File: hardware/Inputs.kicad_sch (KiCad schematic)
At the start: 34 parts, among them J13 Conn_01x05, J14 Conn_01x05, J15 Conn_01x05, J16 Conn_01x05, J17 Conn_01x05, J18 Conn_01x05, J19 Conn_01x03, J20 Conn_01x03, J21 Conn_01x03, J22 Conn_01x03, J23 Conn_01x03, J24 Conn_01x03, J25 Conn_01x02, J26 Conn_01x02, J27 FTSH-107-01-L-D-K

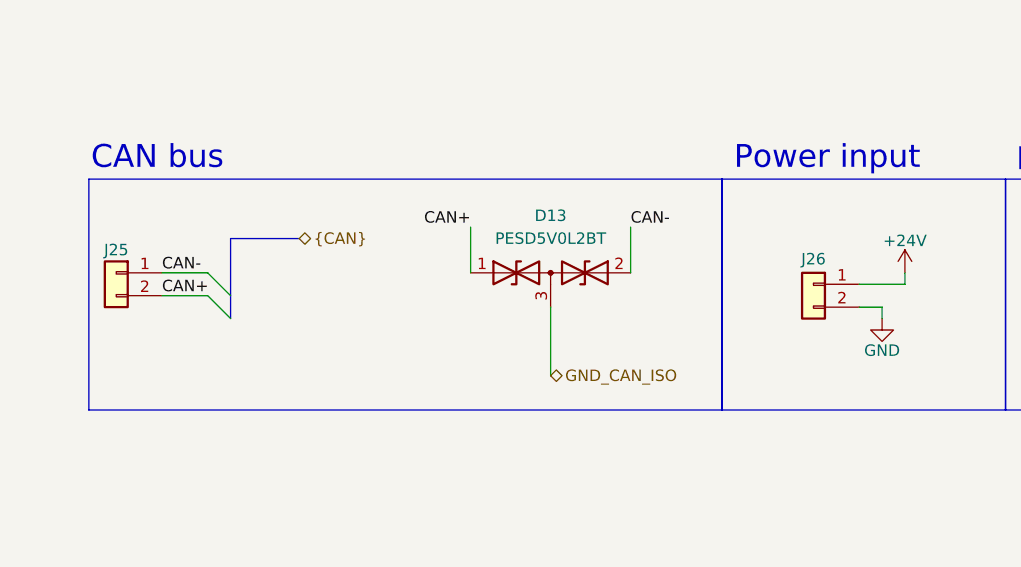
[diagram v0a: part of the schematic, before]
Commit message: Finished components placement on PCB
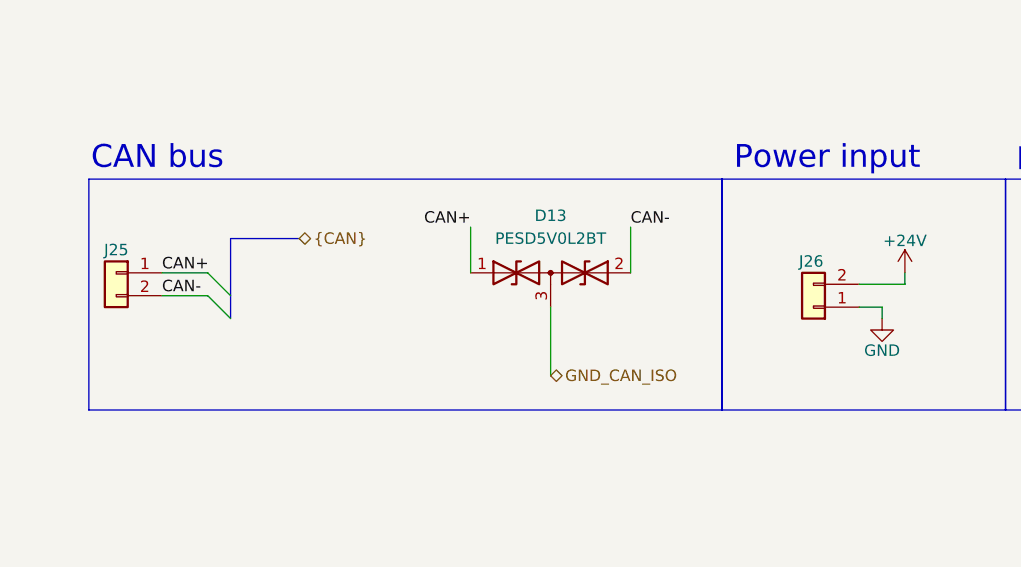
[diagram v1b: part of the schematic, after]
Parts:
- J25, J26: footprint Wago_01x02:26011102 -> StrainRelief:Wire_StrainRelief
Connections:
- net +24V: now also J26.2 (Pin_2); no longer J26.1 (Pin_1)
- net CAN+: now also J25.1 (Pin_1); no longer J25.2 (Pin_2)
- net CAN-: now also J25.2 (Pin_2); no longer J25.1 (Pin_1)
- net GND: now also J26.1 (Pin_1); no longer J26.2 (Pin_2)
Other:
- moved on the sheet: J26
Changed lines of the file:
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@@
 	(wire
 		(pts
+			(xy 190.5 160.02) (xy 195.58 160.02)
+		)
+		(stroke
+			(width 0)
+			(type default)
+		)
+	)
+	(wire
+		(pts
 			(xy 302.26 82.55) (xy 302.26 85.09)
 		)
@@
 	(wire
 		(pts
-			(xy 190.5 160.02) (xy 195.58 160.02)
-		)
-		(stroke
-			(width 0)
-			(type default)
-		)
-	)
-	(wire
-		(pts
-			(xy 190.5 162.56) (xy 195.58 162.56)
+			(xy 267.97 161.29) (xy 273.05 161.29)
 		)
 		(stroke
@@
 		)
 	)
-	(wire
-		(pts
-			(xy 267.97 163.83) (xy 270.51 163.83)
-		)
-		(stroke
-			(width 0)
-			(type default)
-		)
-	)
 	(bus
 		(pts
@@
 	(wire
 		(pts
+			(xy 267.97 163.83) (xy 270.51 163.83)
+		)
+		(stroke
+			(width 0)
+			(type default)
+		)
+	)
+	(wire
+		(pts
 			(xy 80.01 212.09) (xy 87.63 212.09)
 		)
@@
 		)
 	)
-	(wire
-		(pts
-			(xy 267.97 161.29) (xy 273.05 161.29)
-		)
-		(stroke
-			(width 0)
-			(type default)
-		)
-	)
 	(bus
 		(pts
@@
 	(wire
 		(pts
+			(xy 190.5 162.56) (xy 195.58 162.56)
+		)
+		(stroke
+			(width 0)
+			(type default)
+		)
+	)
+	(wire
+		(pts
 			(xy 101.6 109.22) (xy 105.41 109.22)
 		)
@@
 	)
 	(label "CAN-"
-		(at 190.5 160.02 0)
+		(at 190.5 162.56 0)
 		(effects
 			(font
@@
 	)
 	(label "CAN+"
-		(at 190.5 162.56 0)
+		(at 190.5 160.02 0)
 		(effects
 			(font
@@
 			)
 		)
-		(property "Datasheet" "https://wago.priintcloud.com/datasheets/2604-1103/en/b87bf34972496b0cc9989b5aee7282f1?attempt=1&signature=9e2143c2bdc0f032c541ec220a7d0518_1h3r4vhsf"
+		(property "Datasheet" "https://wago.priintcloud.com/datasheets/2601-1103/en/d41d8cd98f00b204e9800998ecf8427e?attempt=1&signature=00012c5e7a2599b3d4b70dcfe3f90a33_1jis4hf1d"
 			(at 24.13 186.69 0)
 			(effects
@@
 			)
 		)
-		(property "Datasheet" "https://wago.priintcloud.com/datasheets/2604-1105/en/b87bf34972496b0cc9989b5aee7282f1?attempt=1&signature=9e2143c2bdc0f032c541ec220a7d0518_1h3r4vhsf"
+		(property "Datasheet" "https://wago.priintcloud.com/datasheets/2601-1105/en/d41d8cd98f00b204e9800998ecf8427e?attempt=1&signature=731afa92f4ad419acfaed54798e1c80c_1jis4e336"
 			(at 96.52 104.14 0)
 			(effects
@@
 			)
 		)
-		(property "Datasheet" "https://wago.priintcloud.com/datasheets/2604-1103/en/b87bf34972496b0cc9989b5aee7282f1?attempt=1&signature=9e2143c2bdc0f032c541ec220a7d0518_1h3r4vhsf"
+		(property "Datasheet" "https://wago.priintcloud.com/datasheets/2601-1103/en/d41d8cd98f00b204e9800998ecf8427e?attempt=1&signature=00012c5e7a2599b3d4b70dcfe3f90a33_1jis4hf1d"
 			(at 24.13 161.29 0)
 			(effects
@@
 		(lib_name "Conn_01x02_1")
 		(lib_id "Connector_Generic:Conn_01x02")
-		(at 262.89 161.29 0)
-		(mirror y)
+		(at 262.89 163.83 180)
 		(unit 1)
 		(exclude_from_sim no)
@@
 		(dnp no)
 		(property "Reference" "J26"
-			(at 262.89 158.496 0)
+			(at 262.636 158.75 0)
 			(effects
 				(font
@@
 		)
 		(property "Value" "Conn_01x02"
-			(at 262.89 167.64 0)
+			(at 262.89 157.48 0)
 			(effects
 				(font
@@
 			)
 		)
-		(property "Footprint" "Wago_01x02:26011102"
-			(at 262.89 161.29 0)
+		(property "Footprint" "StrainRelief:Wire_StrainRelief"
+			(at 262.89 163.83 0)
 			(effects
 				(font
@@
 			)
 		)
-		(property "Datasheet" "https://wago.priintcloud.com/datasheets/2604-1102/en/b87bf34972496b0cc9989b5aee7282f1?attempt=1&signature=9e2143c2bdc0f032c541ec220a7d0518_1h3r4vhsf"
-			(at 262.89 161.29 0)
+		(property "Datasheet" "-"
+			(at 262.89 163.83 0)
 			(effects
 				(font
@@
 		)
 		(property "Description" "Power input"
-			(at 262.89 161.29 0)
+			(at 262.89 163.83 0)
 			(effects
 				(font
@@
 			)
 		)
-		(property "Datasheet" "https://wago.priintcloud.com/datasheets/2604-1103/en/b87bf34972496b0cc9989b5aee7282f1?attempt=1&signature=9e2143c2bdc0f032c541ec220a7d0518_1h3r4vhsf"
+		(property "Datasheet" "https://wago.priintcloud.com/datasheets/2601-1103/en/d41d8cd98f00b204e9800998ecf8427e?attempt=1&signature=00012c5e7a2599b3d4b70dcfe3f90a33_1jis4hf1d"
 			(at 74.93 212.09 0)
 			(effects
@@
 			)
 		)
-		(property "Datasheet" "https://wago.priintcloud.com/datasheets/2604-1105/en/b87bf34972496b0cc9989b5aee7282f1?attempt=1&signature=9e2143c2bdc0f032c541ec220a7d0518_1h3r4vhsf"
+		(property "Datasheet" "https://wago.priintcloud.com/datasheets/2601-1105/en/d41d8cd98f00b204e9800998ecf8427e?attempt=1&signature=731afa92f4ad419acfaed54798e1c80c_1jis4e336"
 			(at 35.56 104.14 0)
 			(effects
@@
 			)
 		)
-		(property "Datasheet" "https://wago.priintcloud.com/datasheets/2604-1105/en/b87bf34972496b0cc9989b5aee7282f1?attempt=1&signature=9e2143c2bdc0f032c541ec220a7d0518_1h3r4vhsf"
+		(property "Datasheet" "https://wago.priintcloud.com/datasheets/2601-1105/en/d41d8cd98f00b204e9800998ecf8427e?attempt=1&signature=731afa92f4ad419acfaed54798e1c80c_1jis4e336"
 			(at 35.56 35.56 0)
 			(effects
@@
 			)
 		)
-		(property "Footprint" "Wago_01x02:26011102"
+		(property "Footprint" "StrainRelief:Wire_StrainRelief"
 			(at 185.42 160.02 0)
 			(effects
@@
 			)
 		)
-		(property "Datasheet" "https://wago.priintcloud.com/datasheets/2604-1102/en/b87bf34972496b0cc9989b5aee7282f1?attempt=1&signature=9e2143c2bdc0f032c541ec220a7d0518_1h3r4vhsf"
+		(property "Datasheet" "-"
 			(at 185.42 160.02 0)
 			(effects
@@
 			)
 		)
-		(property "Datasheet" "https://wago.priintcloud.com/datasheets/2604-1105/en/b87bf34972496b0cc9989b5aee7282f1?attempt=1&signature=9e2143c2bdc0f032c541ec220a7d0518_1h3r4vhsf"
+		(property "Datasheet" "https://wago.priintcloud.com/datasheets/2601-1105/en/d41d8cd98f00b204e9800998ecf8427e?attempt=1&signature=731afa92f4ad419acfaed54798e1c80c_1jis4e336"
 			(at 35.56 68.58 0)
 			(effects
@@
 			)
 		)
-		(property "Datasheet" "https://wago.priintcloud.com/datasheets/2604-1103/en/b87bf34972496b0cc9989b5aee7282f1?attempt=1&signature=9e2143c2bdc0f032c541ec220a7d0518_1h3r4vhsf"
+		(property "Datasheet" "https://wago.priintcloud.com/datasheets/2601-1103/en/d41d8cd98f00b204e9800998ecf8427e?attempt=1&signature=00012c5e7a2599b3d4b70dcfe3f90a33_1jis4hf1d"
 			(at 74.93 186.69 0)
 			(effects
@@
 			)
 		)
-		(property "Datasheet" "https://wago.priintcloud.com/datasheets/2604-1103/en/b87bf34972496b0cc9989b5aee7282f1?attempt=1&signature=9e2143c2bdc0f032c541ec220a7d0518_1h3r4vhsf"
+		(property "Datasheet" "https://wago.priintcloud.com/datasheets/2601-1103/en/d41d8cd98f00b204e9800998ecf8427e?attempt=1&signature=00012c5e7a2599b3d4b70dcfe3f90a33_1jis4hf1d"
 			(at 24.13 212.09 0)
 			(effects
@@
 			)
 		)
-		(property "Datasheet" "https://wago.priintcloud.com/datasheets/2604-1105/en/b87bf34972496b0cc9989b5aee7282f1?attempt=1&signature=9e2143c2bdc0f032c541ec220a7d0518_1h3r4vhsf"
+		(property "Datasheet" "https://wago.priintcloud.com/datasheets/2601-1105/en/d41d8cd98f00b204e9800998ecf8427e?attempt=1&signature=731afa92f4ad419acfaed54798e1c80c_1jis4e336"
 			(at 96.52 35.56 0)
 			(effects
@@
 			)
 		)
-		(property "Datasheet" "https://wago.priintcloud.com/datasheets/2604-1103/en/b87bf34972496b0cc9989b5aee7282f1?attempt=1&signature=9e2143c2bdc0f032c541ec220a7d0518_1h3r4vhsf"
+		(property "Datasheet" "https://wago.priintcloud.com/datasheets/2601-1103/en/d41d8cd98f00b204e9800998ecf8427e?attempt=1&signature=00012c5e7a2599b3d4b70dcfe3f90a33_1jis4hf1d"
 			(at 74.93 161.29 0)
 			(effects
@@
 			)
 		)
-		(property "Datasheet" "https://wago.priintcloud.com/datasheets/2604-1105/en/b87bf34972496b0cc9989b5aee7282f1?attempt=1&signature=9e2143c2bdc0f032c541ec220a7d0518_1h3r4vhsf"
+		(property "Datasheet" "https://wago.priintcloud.com/datasheets/2601-1105/en/d41d8cd98f00b204e9800998ecf8427e?attempt=1&signature=731afa92f4ad419acfaed54798e1c80c_1jis4e336"
 			(at 96.52 68.58 0)
 			(effects

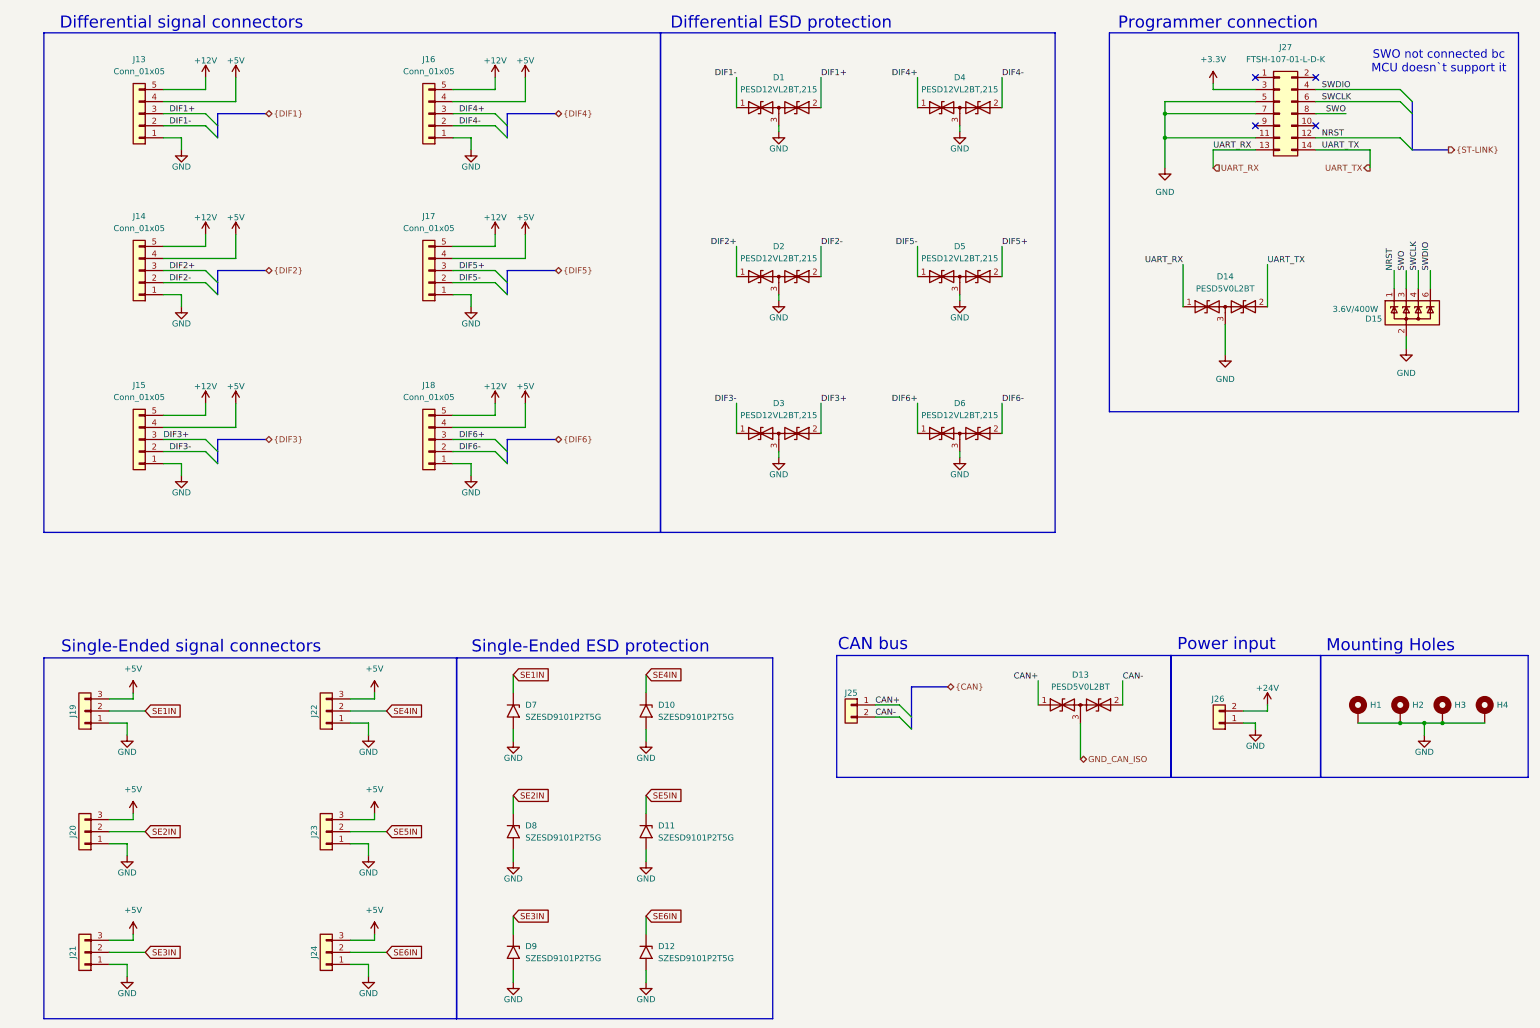
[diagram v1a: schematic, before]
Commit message: Finished routing on PCB
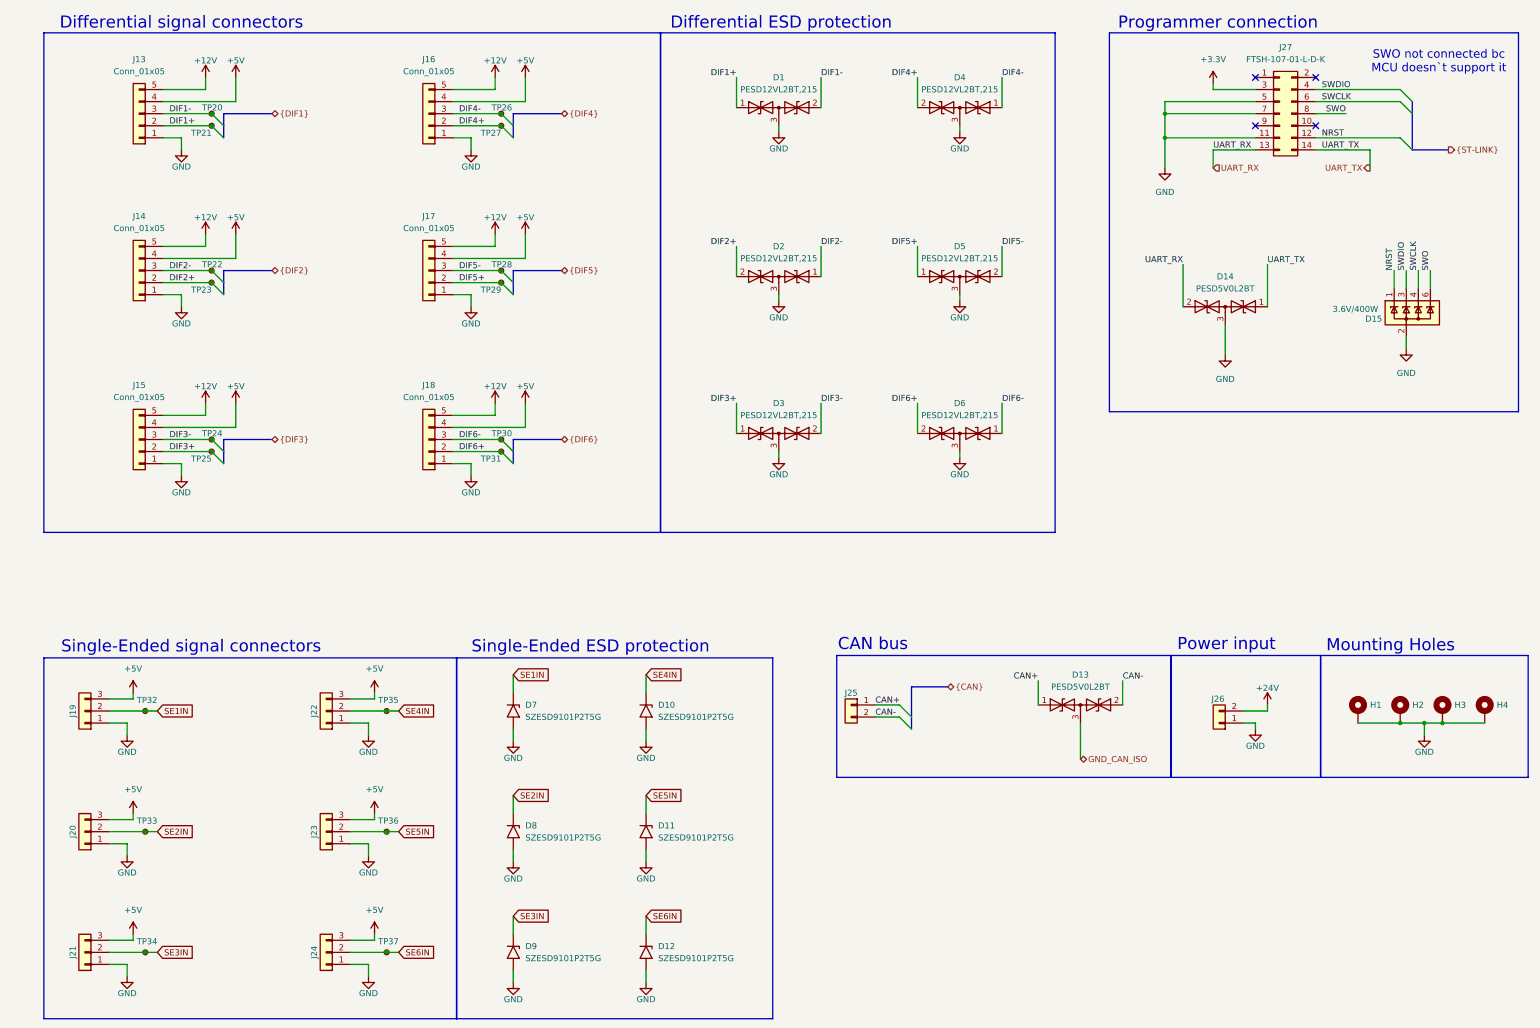
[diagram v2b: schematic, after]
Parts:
- added TP20, TP21, TP22, TP23, TP24, TP25, TP26, TP27, TP28, TP29, TP30, TP31, TP32, TP33, TP34, TP35, TP36, TP37: TestPoint_Small, TestPoint:TestPoint_THTPad_D1.0mm_Drill0.5mm, symbol Connector:TestPoint_Small
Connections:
- net DIF1+: now also D1.1 (A1), J13.2 (Pin_2), TP21.1; no longer D1.2 (A2), J13.3 (Pin_3)
- net DIF1-: now also D1.2 (A2), J13.3 (Pin_3), TP20.1; no longer D1.1 (A1), J13.2 (Pin_2)
- net DIF2+: now also D2.2 (A2), J14.2 (Pin_2), TP23.1; no longer D2.1 (A1), J14.3 (Pin_3)
- net DIF2-: now also D2.1 (A1), J14.3 (Pin_3), TP22.1; no longer D2.2 (A2), J14.2 (Pin_2)
- net DIF3+: now also D3.1 (A1), J15.2 (Pin_2), TP25.1; no longer D3.2 (A2), J15.3 (Pin_3)
- net DIF3-: now also D3.2 (A2), J15.3 (Pin_3), TP24.1; no longer D3.1 (A1), J15.2 (Pin_2)
- net DIF4+: now also D4.2 (A2), J16.2 (Pin_2), TP27.1; no longer D4.1 (A1), J16.3 (Pin_3)
- net DIF4-: now also D4.1 (A1), J16.3 (Pin_3), TP26.1; no longer D4.2 (A2), J16.2 (Pin_2)
- net DIF5+: now also D5.1 (A1), J17.2 (Pin_2), TP29.1; no longer D5.2 (A2), J17.3 (Pin_3)
- net DIF5-: now also D5.2 (A2), J17.3 (Pin_3), TP28.1; no longer D5.1 (A1), J17.2 (Pin_2)
- net DIF6+: now also D6.2 (A2), J18.2 (Pin_2), TP31.1; no longer D6.1 (A1), J18.3 (Pin_3)
- net DIF6-: now also D6.1 (A1), J18.3 (Pin_3), TP30.1; no longer D6.2 (A2), J18.2 (Pin_2)
- net SE1IN: now also TP32.1
- net SE2IN: now also TP33.1
- net SE3IN: now also TP34.1
- net SE4IN: now also TP35.1
- net SE5IN: now also TP36.1
- net SE6IN: now also TP37.1
- net SWDIO: now also D15.3 (K); no longer D15.6 (K)
- net SWO: now also D15.6 (K); no longer D15.3 (K)
- net UART_RX: now also D14.2 (A2); no longer D14.1 (A1)
- net UART_TX: now also D14.1 (A1); no longer D14.2 (A2)

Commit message: Added description, fixed engineering fee
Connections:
- net DIF1+: now also TP20.1; no longer TP21.1
- net DIF1-: now also TP21.1; no longer TP20.1
- net DIF3+: now also TP24.1; no longer TP25.1
- net DIF3-: now also TP25.1; no longer TP24.1
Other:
- moved on the sheet: TP20, TP21, TP24, TP25
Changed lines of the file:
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@@
 	)
 	(junction
-		(at 50.8 38.1)
-		(diameter 0)
-		(color 0 0 0 0)
-	)
-	(junction
 		(at 309.88 163.83)
 		(diameter 0)
@@
 	)
 	(junction
-		(at 50.8 106.68)
+		(at 36.83 161.29)
 		(diameter 0)
 		(color 0 0 0 0)
 	)
 	(junction
-		(at 36.83 161.29)
+		(at 50.8 35.56)
 		(diameter 0)
 		(color 0 0 0 0)
@@
 	)
 	(junction
+		(at 50.8 104.14)
+		(diameter 0)
+		(color 0 0 0 0)
+	)
+	(junction
 		(at 111.76 68.58)
 		(diameter 0)
@@
 	)
 	(junction
-		(at 111.76 35.56)
+		(at 50.8 38.1)
 		(diameter 0)
 		(color 0 0 0 0)
 	)
 	(junction
-		(at 50.8 104.14)
+		(at 111.76 35.56)
 		(diameter 0)
 		(color 0 0 0 0)
 	)
 	(junction
-		(at 111.76 106.68)
+		(at 50.8 106.68)
 		(diameter 0)
 		(color 0 0 0 0)
 	)
 	(junction
-		(at 50.8 35.56)
+		(at 111.76 106.68)
 		(diameter 0)
 		(color 0 0 0 0)
@@
 	(symbol
 		(lib_id "Connector:TestPoint_Small")
-		(at 50.8 104.14 0)
+		(at 50.8 106.68 0)
 		(unit 1)
 		(exclude_from_sim no)
@@
 		(dnp no)
 		(property "Reference" "TP24"
-			(at 48.768 102.87 0)
+			(at 45.974 108.204 0)
 			(effects
 				(font
@@
 		)
 		(property "Value" "TestPoint_Small"
-			(at 52.07 105.4099 0)
+			(at 52.07 107.9499 0)
 			(effects
 				(font
@@
 		)
 		(property "Footprint" "TestPoint:TestPoint_THTPad_D1.0mm_Drill0.5mm"
-			(at 55.88 104.14 0)
+			(at 55.88 106.68 0)
 			(effects
 				(font
@@
 		)
 		(property "Datasheet" "~"
-			(at 55.88 104.14 0)
+			(at 55.88 106.68 0)
 			(effects
 				(font
@@
 		)
 		(property "Description" "test point"
-			(at 50.8 104.14 0)
+			(at 50.8 106.68 0)
 			(effects
 				(font
@@
 	(symbol
 		(lib_id "Connector:TestPoint_Small")
-		(at 50.8 35.56 0)
+		(at 50.8 38.1 0)
 		(unit 1)
 		(exclude_from_sim no)
@@
 		(dnp no)
 		(property "Reference" "TP20"
-			(at 48.768 34.29 0)
+			(at 46.228 39.624 0)
 			(effects
 				(font
@@
 		)
 		(property "Value" "TestPoint_Small"
-			(at 52.07 36.8299 0)
+			(at 52.07 39.3699 0)
 			(effects
 				(font
@@
 		)
 		(property "Footprint" "TestPoint:TestPoint_THTPad_D1.0mm_Drill0.5mm"
-			(at 55.88 35.56 0)
+			(at 55.88 38.1 0)
 			(effects
 				(font
@@
 		)
 		(property "Datasheet" "~"
-			(at 55.88 35.56 0)
+			(at 55.88 38.1 0)
 			(effects
 				(font
@@
 		)
 		(property "Description" "test point"
-			(at 50.8 35.56 0)
+			(at 50.8 38.1 0)
 			(effects
 				(font
@@
 	(symbol
 		(lib_id "Connector:TestPoint_Small")
-		(at 50.8 106.68 0)
+		(at 50.8 104.14 0)
 		(unit 1)
 		(exclude_from_sim no)
@@
 		(dnp no)
 		(property "Reference" "TP25"
-			(at 46.482 108.204 0)
+			(at 48.514 102.616 0)
 			(effects
 				(font
@@
 		)
 		(property "Value" "TestPoint_Small"
-			(at 52.07 107.9499 0)
+			(at 52.07 105.4099 0)
 			(effects
 				(font
@@
 		)
 		(property "Footprint" "TestPoint:TestPoint_THTPad_D1.0mm_Drill0.5mm"
-			(at 55.88 106.68 0)
+			(at 55.88 104.14 0)
 			(effects
 				(font
@@
 		)
 		(property "Datasheet" "~"
-			(at 55.88 106.68 0)
+			(at 55.88 104.14 0)
 			(effects
 				(font
@@
 		)
 		(property "Description" "test point"
-			(at 50.8 106.68 0)
+			(at 50.8 104.14 0)
 			(effects
 				(font
@@
 	(symbol
 		(lib_id "Connector:TestPoint_Small")
-		(at 50.8 38.1 0)
+		(at 50.8 35.56 0)
 		(unit 1)
 		(exclude_from_sim no)
@@
 		(dnp no)
 		(property "Reference" "TP21"
-			(at 46.482 39.624 0)
+			(at 48.768 34.29 0)
 			(effects
 				(font
@@
 		)
 		(property "Value" "TestPoint_Small"
-			(at 52.07 39.3699 0)
+			(at 52.07 36.8299 0)
 			(effects
 				(font
@@
 		)
 		(property "Footprint" "TestPoint:TestPoint_THTPad_D1.0mm_Drill0.5mm"
-			(at 55.88 38.1 0)
+			(at 55.88 35.56 0)
 			(effects
 				(font
@@
 		)
 		(property "Datasheet" "~"
-			(at 55.88 38.1 0)
+			(at 55.88 35.56 0)
 			(effects
 				(font
@@
 		)
 		(property "Description" "test point"
-			(at 50.8 38.1 0)
+			(at 50.8 35.56 0)
 			(effects
 				(font
